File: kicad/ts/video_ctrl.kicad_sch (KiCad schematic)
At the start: 14 parts, among them U1 74LS93

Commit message: update footprints
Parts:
- F1, G1, G10, G2, G3, G6, G8, G9, U1: footprint (none) -> Package_DIP:DIP-14_W7.62mm
- N1, N2, N3, N4: footprint Package_DIP:DIP-14_W7.62mm -> Package_DIP:DIP-16_W7.62mm
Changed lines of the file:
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@@
 			)
 		)
-		(property "Footprint" ""
+		(property "Footprint" "Package_DIP:DIP-14_W7.62mm"
 			(at 92.71 201.93 0)
 			(effects
@@
 			)
 		)
-		(property "Footprint" ""
+		(property "Footprint" "Package_DIP:DIP-14_W7.62mm"
 			(at 93.345 191.135 0)
 			(effects
@@
 			)
 		)
-		(property "Footprint" "Package_DIP:DIP-14_W7.62mm"
+		(property "Footprint" "Package_DIP:DIP-16_W7.62mm"
 			(at 53.975 109.22 0)
 			(effects
@@
 			)
 		)
-		(property "Footprint" ""
+		(property "Footprint" "Package_DIP:DIP-14_W7.62mm"
 			(at 116.205 225.425 0)
 			(effects
@@
 			)
 		)
-		(property "Footprint" ""
+		(property "Footprint" "Package_DIP:DIP-14_W7.62mm"
 			(at 93.345 182.245 0)
 			(effects
@@
 			)
 		)
-		(property "Footprint" ""
+		(property "Footprint" "Package_DIP:DIP-14_W7.62mm"
 			(at 46.355 192.405 0)
 			(effects
@@
 			)
 		)
-		(property "Footprint" ""
+		(property "Footprint" "Package_DIP:DIP-14_W7.62mm"
 			(at 67.945 210.185 0)
 			(effects
@@
 			)
 		)
-		(property "Footprint" "Package_DIP:DIP-14_W7.62mm"
+		(property "Footprint" "Package_DIP:DIP-16_W7.62mm"
 			(at 78.74 46.355 0)
 			(effects
@@
 			)
 		)
-		(property "Footprint" "Package_DIP:DIP-14_W7.62mm"
+		(property "Footprint" "Package_DIP:DIP-16_W7.62mm"
 			(at 125.095 46.355 0)
 			(effects
@@
 			)
 		)
-		(property "Footprint" ""
+		(property "Footprint" "Package_DIP:DIP-14_W7.62mm"
 			(at 112.395 237.49 0)
 			(effects
@@
 			)
 		)
-		(property "Footprint" ""
+		(property "Footprint" "Package_DIP:DIP-14_W7.62mm"
 			(at 116.205 156.21 0)
 			(effects
@@
 			)
 		)
-		(property "Footprint" ""
+		(property "Footprint" "Package_DIP:DIP-14_W7.62mm"
 			(at 67.945 161.29 0)
 			(effects
@@
 			)
 		)
-		(property "Footprint" ""
+		(property "Footprint" "Package_DIP:DIP-14_W7.62mm"
 			(at 160.02 107.315 0)
 			(effects
@@
 			)
 		)
-		(property "Footprint" ""
+		(property "Footprint" "Package_DIP:DIP-14_W7.62mm"
 			(at 67.945 188.595 0)
 			(effects
@@
 			)
 		)
-		(property "Footprint" ""
+		(property "Footprint" "Package_DIP:DIP-14_W7.62mm"
 			(at 92.71 158.75 0)
 			(effects
@@
 			)
 		)
-		(property "Footprint" "Package_DIP:DIP-14_W7.62mm"
+		(property "Footprint" "Package_DIP:DIP-16_W7.62mm"
 			(at 100.33 109.22 0)
 			(effects
@@
 			)
 		)
-		(property "Footprint" ""
+		(property "Footprint" "Package_DIP:DIP-14_W7.62mm"
 			(at 92.71 170.815 0)
 			(effects
@@
 			)
 		)
-		(property "Footprint" ""
+		(property "Footprint" "Package_DIP:DIP-14_W7.62mm"
 			(at 92.71 212.725 0)
 			(effects
@@
 			)
 		)
-		(property "Footprint" ""
+		(property "Footprint" "Package_DIP:DIP-14_W7.62mm"
 			(at 46.355 237.49 0)
 			(effects
@@
 			)
 		)
-		(property "Footprint" ""
+		(property "Footprint" "Package_DIP:DIP-14_W7.62mm"
 			(at 88.265 222.885 0)
 			(effects
@@
 			)
 		)
-		(property "Footprint" ""
+		(property "Footprint" "Package_DIP:DIP-14_W7.62mm"
 			(at 161.925 202.565 0)
 			(effects
@@
 			)
 		)
-		(property "Footprint" ""
+		(property "Footprint" "Package_DIP:DIP-14_W7.62mm"
 			(at 161.925 183.515 0)
 			(effects

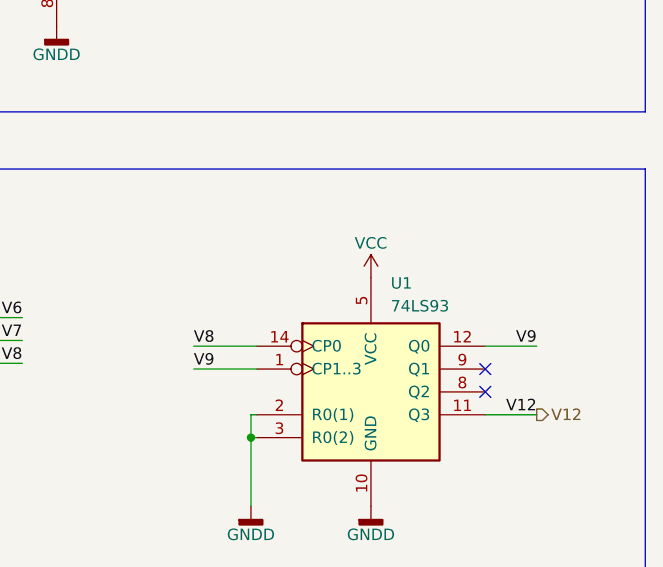
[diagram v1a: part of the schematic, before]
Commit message: Schemativ corrections, work started on pcb
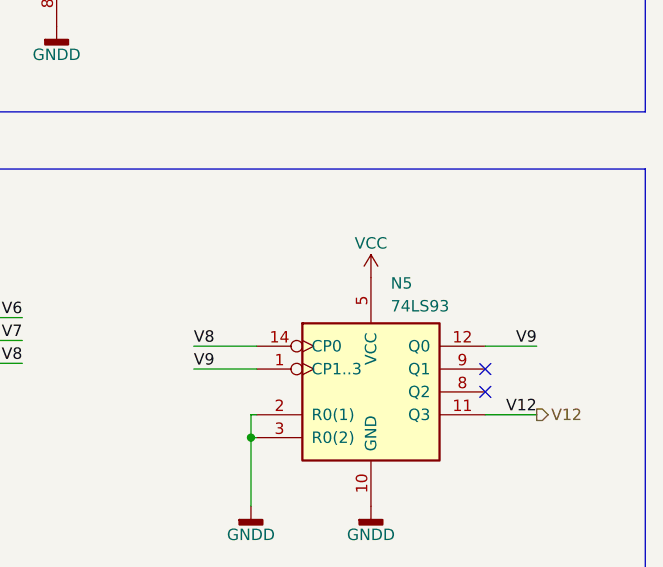
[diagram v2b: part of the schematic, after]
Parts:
- G5: footprint (none) -> Package_DIP:DIP-14_W7.62mm
- renumbered U1 to N5
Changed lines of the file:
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@@
 			)
 		)
-		(property "Footprint" ""
+		(property "Footprint" "Package_DIP:DIP-14_W7.62mm"
 			(at 116.205 204.47 0)
 			(effects
@@
 		(dnp no)
 		(fields_autoplaced yes)
-		(property "Reference" "U1"
+		(property "Reference" "N5"
 			(at 162.2141 95.25 0)
 			(effects
@@
 			(project ""
 				(path "/13135b82-690b-4b84-a983-6756320cca7f/27c04af6-a892-4501-9f89-03b445cabf22"
-					(reference "U1")
+					(reference "N5")
 					(unit 1)
 				)
@@
 			)
 		)
-		(property "Footprint" ""
+		(property "Footprint" "Package_DIP:DIP-14_W7.62mm"
 			(at 67.945 222.885 0)
 			(effects
@@
 			)
 		)
-		(property "Footprint" ""
+		(property "Footprint" "Package_DIP:DIP-14_W7.62mm"
 			(at 116.205 184.785 0)
 			(effects

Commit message: Schematic corrections, add more pcb traces
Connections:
- net H5: now also G2.1; no longer G2.2
- net ~{PVB}: now also G2.2; no longer G2.1
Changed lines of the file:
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@@
 		(lib_id "74xx:74LS08")
 		(at 116.205 225.425 0)
+		(mirror x)
 		(unit 1)
 		(exclude_from_sim no)
@@
 		)
 		(property "Value" "74LS08"
-			(at 115.57 230.505 0)
+			(at 115.57 220.345 0)
 			(effects
 				(font

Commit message: Last schema & pcb corrections, DRC passed, some warnings todo
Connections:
- net GCK: now also F1.3 (C)
- net GNDD: no longer F1.3 (C)
- net VCC: no longer N3.1 (B), N3.10 (C), N3.15 (A), N3.9 (D), N4.1 (B), N4.10 (C), N4.15 (A), N4.9 (D)
- no-connect marks 9 -> 17
